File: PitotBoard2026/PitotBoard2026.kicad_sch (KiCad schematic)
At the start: 61 parts, among them J1 RJ25, J2 ICSP(, J3 Conn_01x04_Socket, J4 Conn_01x04_Pin, J5 Conn_01x04_Socket, J6 Conn_01x04_Pin, SW1 RST, U1 ATmega328PB-A, U10 MCP25625-x-SS, U11 FXMA2102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

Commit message: Add files via upload
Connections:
- net GND: now also U10.26 (VSS)
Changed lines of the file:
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@@
+	)
+	(junction
+		(at 209.55 85.09)
+		(diameter 0)
+		(color 0 0 0 0)
 	)
 	(junction
@@
 		)
 		(stroke
+			(width 0)
+			(type default)
+		)
+	)
+	(wire
+		(pts
+			(xy 209.55 85.09) (xy 217.17 85.09)
+		)
+		(stroke

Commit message: Add files via upload
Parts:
- J2: value ICSP( -> ICSP
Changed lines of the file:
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@@
 			)
 		)
-		(property "Value" "ICSP("
+		(property "Value" "ICSP"
 			(at -6.985 142.24 0)
 			(effects

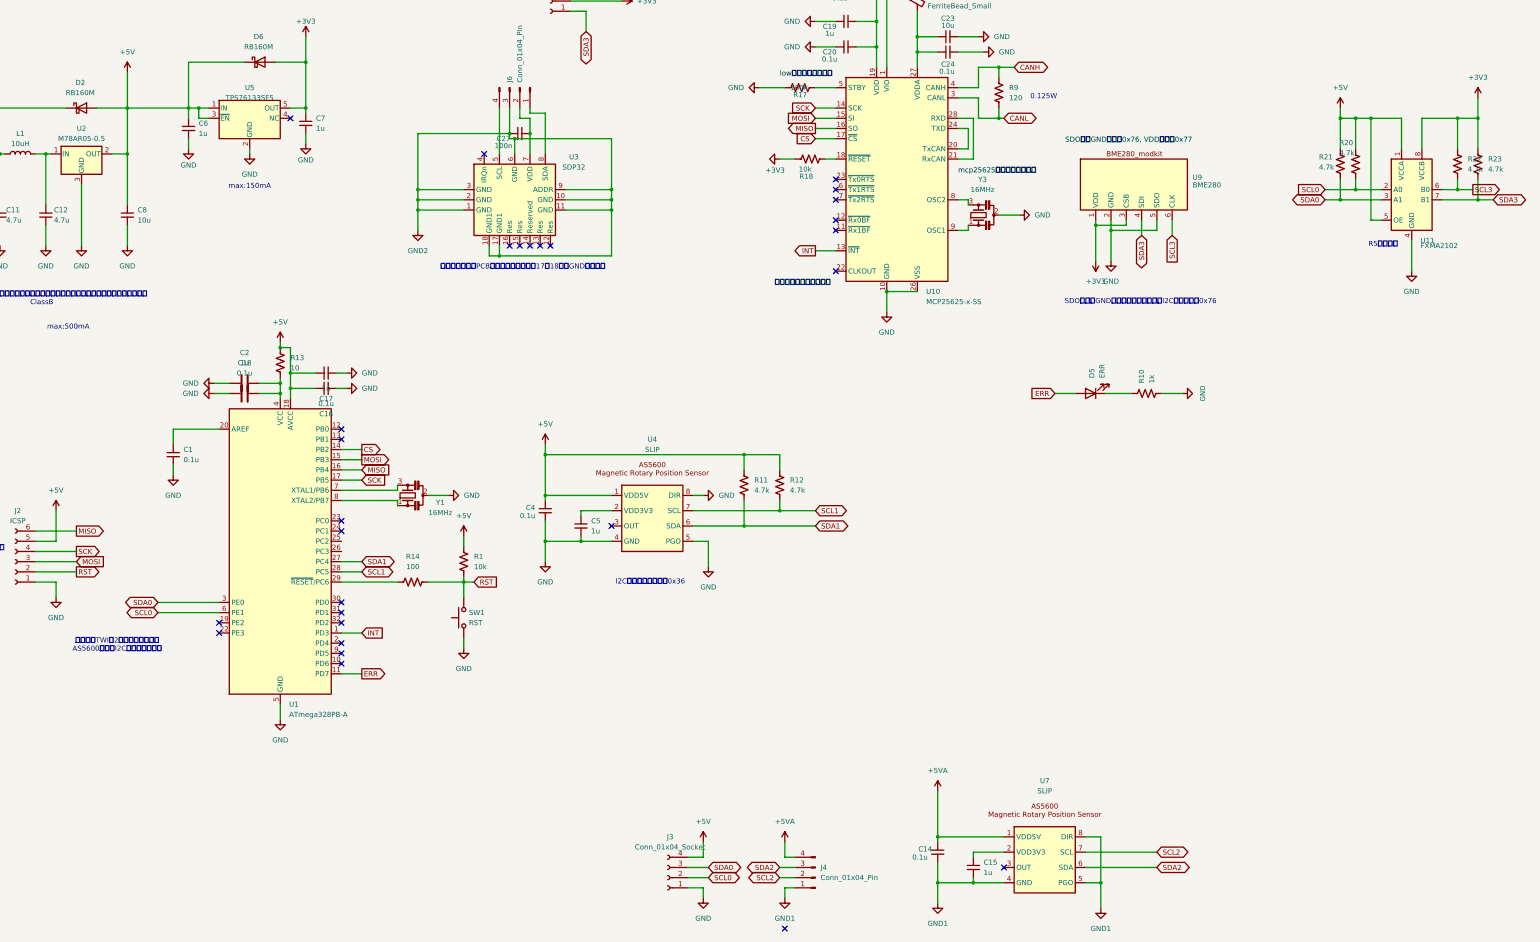
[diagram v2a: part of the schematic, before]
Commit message: Add files via upload
FXMA2102とM78ARのフットプリントを修正
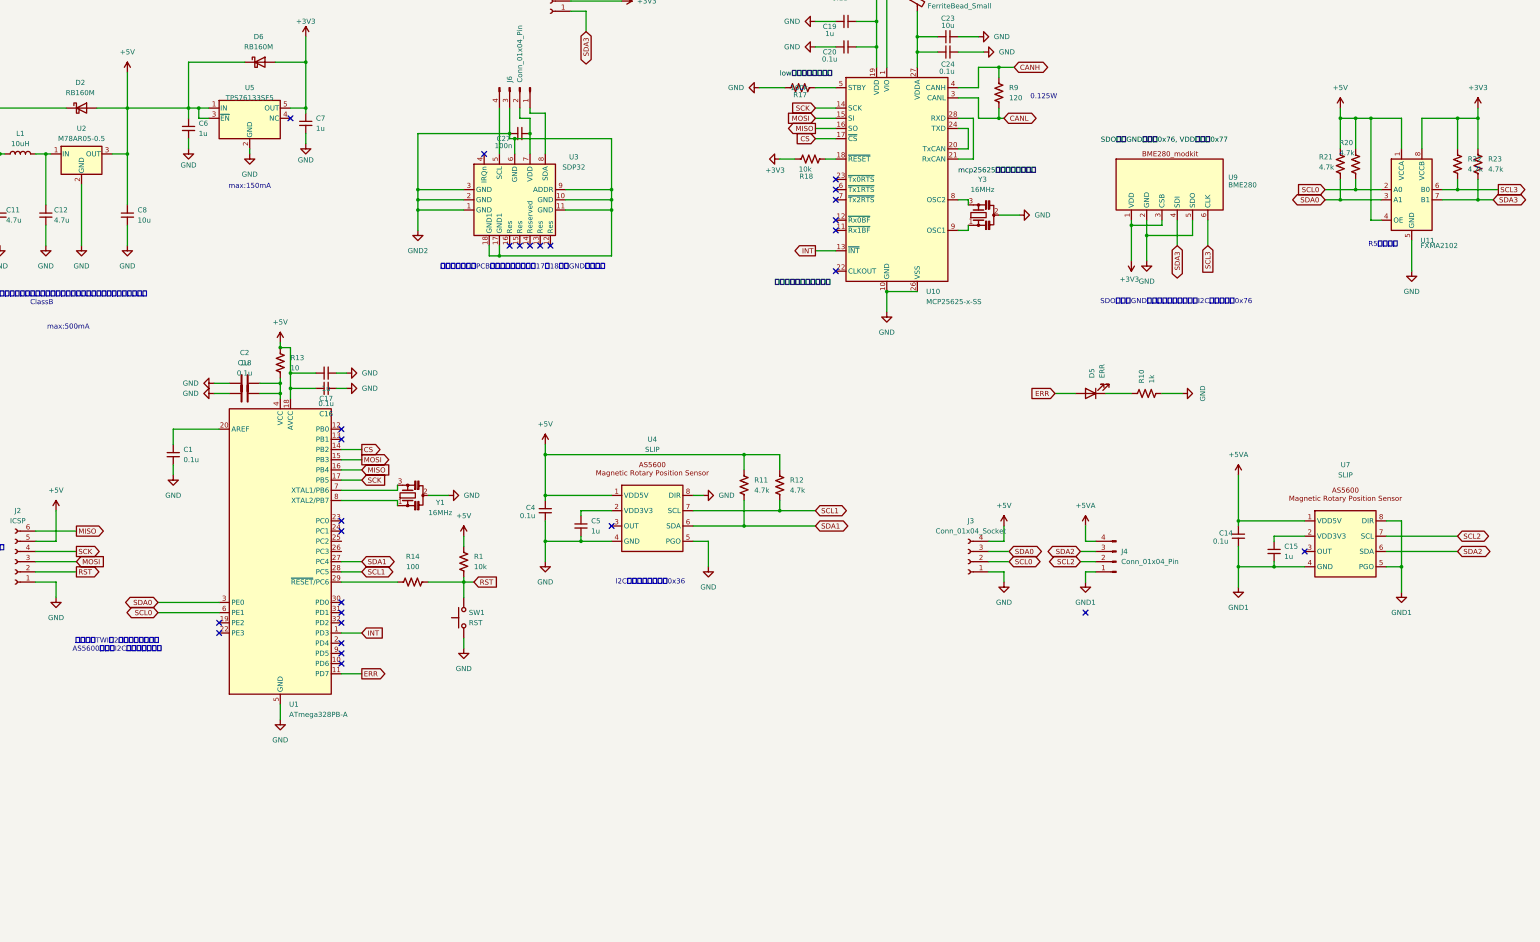
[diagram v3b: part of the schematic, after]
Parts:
- U2: footprint Package_SIP:SIP3_11.6x8.5mm -> KUBTSS:SIP3_11.6x8.5mm
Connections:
- net +5V: now also U11.4 (OE), U2.3 (OUT); no longer U11.5 (OE), U2.2 (OUT)
- net GND: now also U11.5 (GND), U2.2 (GND); no longer U11.4 (GND), U2.3 (GND)
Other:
- moved on the sheet: C14, C15, J3, J4, U7, U9

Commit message: Add files via upload
MCP25625を5Vに変更。FXMA2102のピン番号を修正。
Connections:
- net +3V3: no longer C21.1, C22.1, R18.2, U10.1 (VIO)
- net +5V: now also C21.1, C22.1, R18.2, U10.1 (VIO)
- net SCL3: now also U11.7 (B0); no longer U11.6 (B0)
- net SDA3: now also U11.6 (B1); no longer U11.7 (B1)
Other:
- note added: "B0 7 B1 6"
- moved on the sheet: C1, C16, C17, C18, C2, C4, C5, J2, R1, R11, R12, R13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
